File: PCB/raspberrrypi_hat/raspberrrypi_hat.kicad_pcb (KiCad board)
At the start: 4 copper layers, 65 x 56 mm, 24 parts, among them J3 40HAT, J6 CONN_02X02, J9 CONN_01X02, Q1 DMG2305UX, Q2 DMMT5401, U1 NeowayM590, U2 CAT24C32

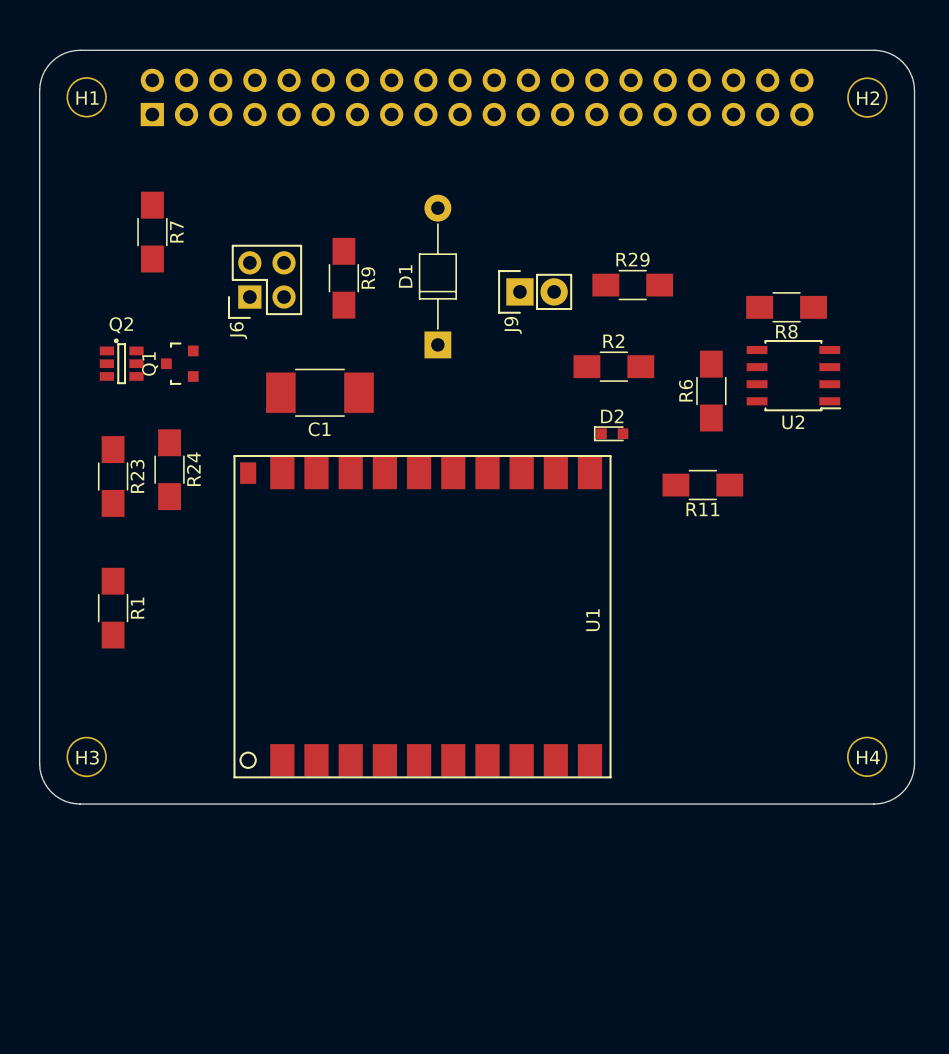
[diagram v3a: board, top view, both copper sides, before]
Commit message: PCB: Change RPi header + add Micro SIM socket. Starting placement
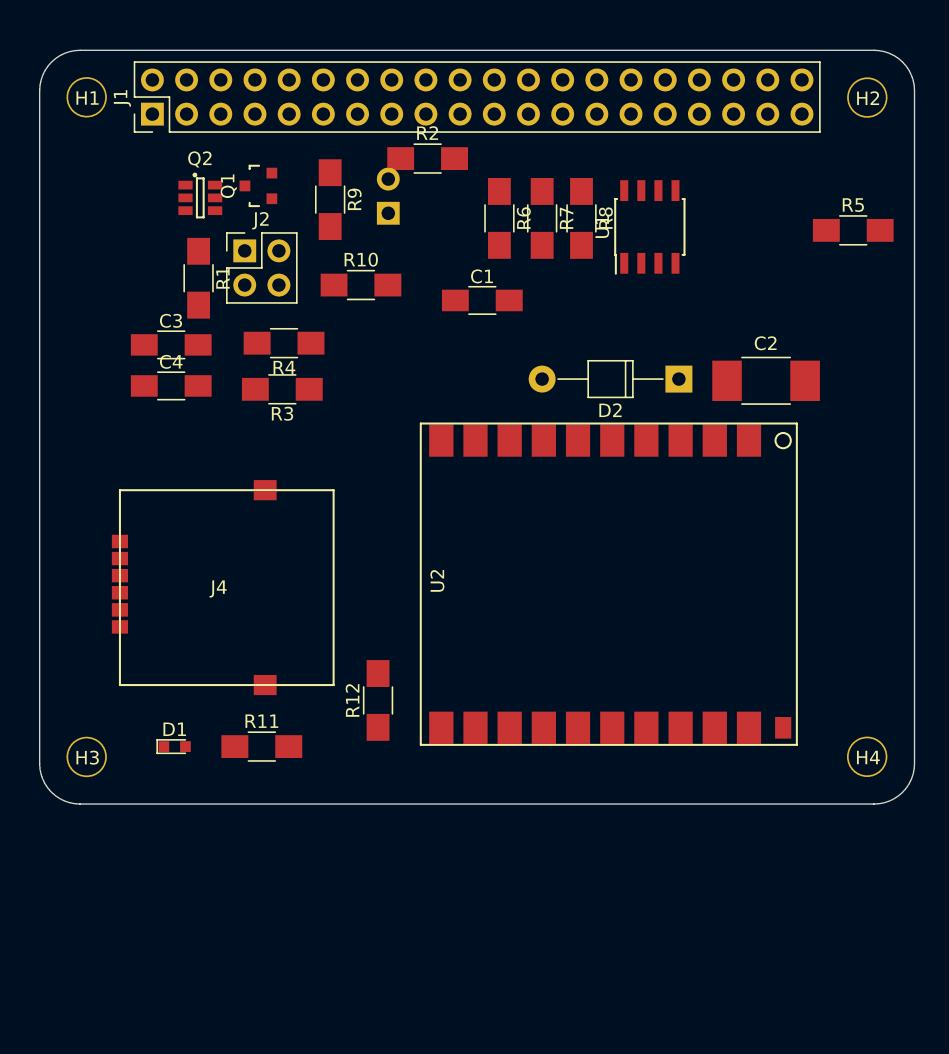
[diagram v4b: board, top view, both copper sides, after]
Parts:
- removed J6: CONN_02X02, Pin_Headers:Pin_Header_Straight_2x02
- removed J9: CONN_01X02, Pin_Headers:Pin_Header_Straight_1x02
- removed R23, R24: 22, Resistors_SMD:R_1206_HandSoldering
- removed R29: 10K, Resistors_SMD:R_1206_HandSoldering
- added C2: 470µF, Capacitors_SMD:C_1812_HandSoldering, F.Cu at (132.5, 85.4)
- added C3: 0.1µF, Capacitors_SMD:C_1206_HandSoldering, F.Cu at (88.3, 82.7)
- added C4: 100pF, Capacitors_SMD:C_1206_HandSoldering, F.Cu at (88.3, 85.8)
- added J1: 40HAT, Pin_Headers:Pin_Header_Straight_2x20_Pitch2.54mm, F.Cu at (86.9, 65.6)
- added J2: CONN_02X02, Pin_Headers:Pin_Header_Straight_2x02_Pitch2.54mm, F.Cu at (93.8, 75.7)
- added J4: Micro_SIM_Card, project_footprints:MicroSIMSocket, F.Cu at (84.5, 100.7)
- added R10: 200, Resistors_SMD:R_1206_HandSoldering, F.Cu at (102.4, 78.3)
- added R12: 10K, Resistors_SMD:R_1206_HandSoldering, F.Cu at (103.7, 109.1)
- added R3: DNP, Resistors_SMD:R_1206_HandSoldering, F.Cu at (96.6, 86.0)
- added R4: DNP, Resistors_SMD:R_1206_HandSoldering, F.Cu at (96.7, 82.6)
- added R5: DNP, Resistors_SMD:R_1206_HandSoldering, F.Cu at (139.0, 74.2)
- C1: value CP -> 100pF; footprint Capacitors_SMD:C_1812_HandSoldering -> Capacitors_SMD:C_1206_HandSoldering
- D1: value D -> LED; footprint Diodes_ThroughHole:D_T-1_P10.16mm_Horizontal -> LEDs:LED_0603
- D2: value LED -> 1N4007; footprint LEDs:LED_0603 -> Diodes_ThroughHole:D_T-1_P10.16mm_Horizontal
- J3: value 40HAT -> CONN_01X02; footprint Socket_Strips:Socket_Strip_Straight_2x20 -> Pin_Headers:Pin_Header_Straight_1x02_Pitch2.54mm
- R1, R2: value R -> 22
- R11: value DNP -> 4.7K
- R6: value 3.9K -> 10K
- R7: value DNP -> 3.9K
- R9: value DNP -> 200
- U1: value NeowayM590 -> CAT24C32; footprint project_footprints:NeowayM590 -> Housings_SOIC:SOIC-8_3.9x4.9mm_Pitch1.27mm
- U2: value CAT24C32 -> NeowayM590; footprint Housings_SOIC:SOIC-8_3.9x4.9mm_Pitch1.27mm -> project_footprints:NeowayM590
- moved U1 48.1 mm to (123.9, 73.9)
- moved R11 38.1 mm to (95.1, 112.5), turned to 0 degrees
- moved D1 35.7 mm to (88.6, 112.5), turned to 0 degrees
- moved R7 29.0 mm to (115.9, 73.3)
- moved R1 25.3 mm to (90.4, 77.8)
- moved R2 20.7 mm to (107.4, 68.9)
- moved R6 20.3 mm to (112.7, 73.3), turned to 270 degrees
- moved J3 19.0 mm to (104.5, 72.9)
- moved R8 16.6 mm to (118.8, 73.3), turned to 270 degrees
- moved Q1 14.4 mm to (94.8, 70.9)
- moved C1 13.9 mm to (111.4, 79.4), turned to 0 degrees
- moved Q2 13.6 mm to (90.5, 71.8)
- moved D2 6.41 mm to (126.0, 85.2), turned to 180 degrees
- moved R9 5.93 mm to (100.1, 71.9)
- moved U2 5.85 mm to (131.2, 89.8), turned to 270 degrees
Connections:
- C1 pad 1: Net-(C1-Pad1) -> /RXD
- D1 pad 1: Net-(C1-Pad1) -> GND
- D1 pad 2: /P5V -> Net-(D1-Pad2)
- D2 pad 1: GND -> /M590/VBAT
- D2 pad 2: Net-(D2-Pad2) -> /P5V
- J3 pad 1: /P3V3_HAT -> GND
- J3 pad 2: /P5V_HAT -> Net-(J3-Pad2)
- R1 pad 1: (no net) -> Net-(Q2-Pad1)
- R1 pad 2: (no net) -> GND
- R11 pad 1: Net-(J9-Pad2) -> Net-(R11-Pad1)
- R11 pad 2: GND -> Net-(D1-Pad2)
- R2 pad 1: (no net) -> Net-(Q1-Pad1)
- R2 pad 2: Net-(D2-Pad2) -> GND
- R6 pad 2: /ID_SD_EEPROM -> Net-(J3-Pad2)
- R7 pad 1: /P3V3_HAT -> /P3V3
- R7 pad 2: /P3V3 -> /ID_SD_EEPROM
- R9 pad 1: /P5V_HAT -> /TXD
- R9 pad 2: /P5V -> /TXD
- U1 pad 2: /P5V -> GND
- U1 pad 3: /P5V -> GND
- U1 pad 4: (no net) -> GND
- U1 pad 5: (no net) -> /ID_SC_EEPROM
- U1 pad 6: (no net) -> /ID_SD_EEPROM
- U1 pad 7: (no net) -> Net-(J3-Pad2)
- U1 pad 8: (no net) -> /P3V3
- U2 pad 2: GND -> /M590/VBAT
- U2 pad 3: GND -> /M590/VBAT
- U2 pad 5: /ID_SC_EEPROM -> Net-(R11-Pad1)
- U2 pad 6: /ID_SD_EEPROM -> (no net)
- U2 pad 7: Net-(J9-Pad2) -> /RXD
- U2 pad 8: /P3V3 -> /TXD
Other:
- board text removed: "If you want to use an SMT 40-pin header, please move the top edge up by 0.5mm and locate the header in the same location as the current TH part."

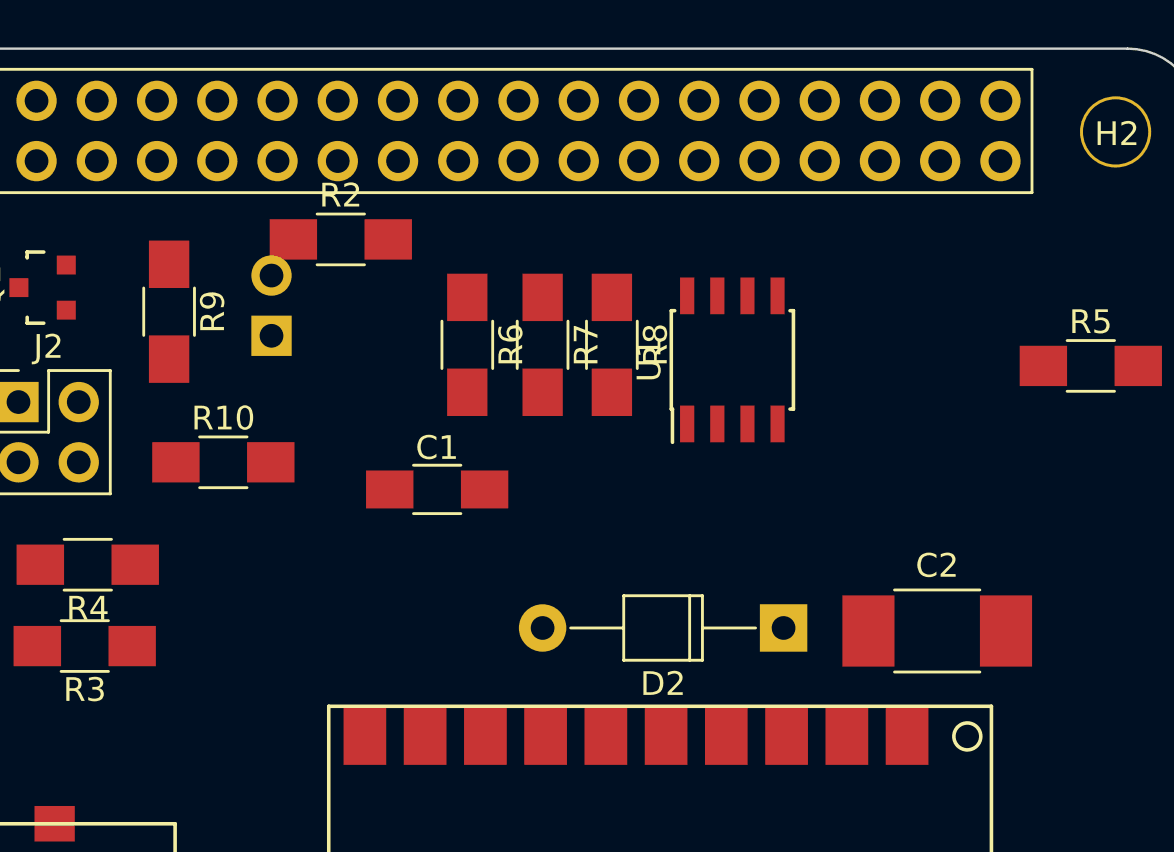
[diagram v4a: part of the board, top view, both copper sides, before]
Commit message: Fix TX/RX serial resistor short-cut by adding mTX/mRX in M590 module sheet
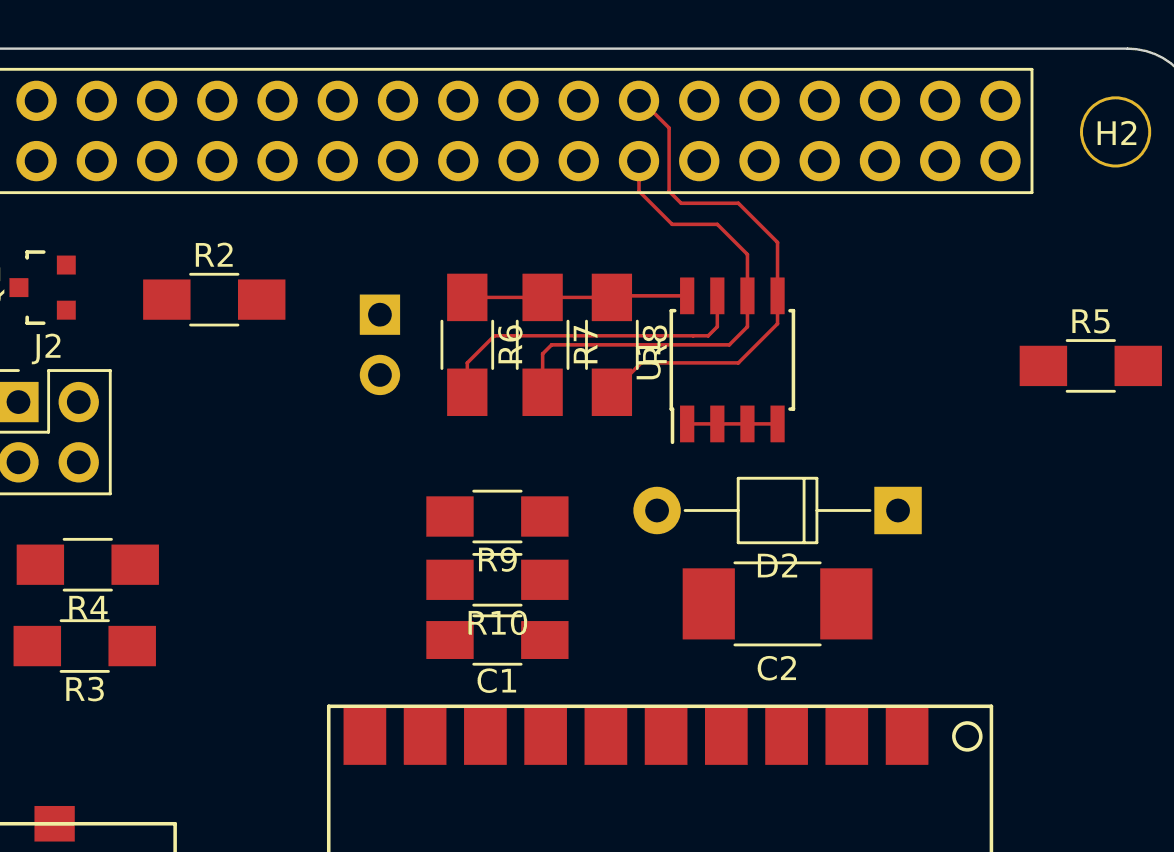
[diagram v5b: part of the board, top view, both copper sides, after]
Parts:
- moved R9 16.3 mm to (114.0, 80.5), turned to 180 degrees
- moved R10 12.6 mm to (114.0, 83.2), turned to 180 degrees
- moved D2 6.92 mm to (130.9, 80.3)
- moved C1 6.84 mm to (114.0, 85.8), turned to 180 degrees
- moved C2 6.83 mm to (125.8, 84.2), turned to 180 degrees
- moved R2 5.91 mm to (102.0, 71.4)
- moved J3 4.66 mm to (109.0, 72.0), turned to 180 degrees
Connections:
- C1 pad 1: /RXD -> /M590/mRXD
- R10 pad 1: /RXD -> /M590/mRXD
- R9 pad 1: /TXD -> /M590/mTXD
- U2 pad 7: /RXD -> /M590/mRXD
- U2 pad 8: /TXD -> /M590/mTXD
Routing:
- net /ID_SC_EEPROM: track 0.11 -> 21.6 mm
- net /ID_SD_EEPROM: track 1.07 -> 21.8 mm
- net Net-(J3-Pad2): track 0.00 -> 13.7 mm
- net /P3V3: track 0.00 -> 9.30 mm
- net GND: track 0.00 -> 3.81 mm

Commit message: PCB: keep on routing
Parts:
- J3: moved to F.Cu
- moved C3 46.0 mm to (133.3, 72.8)
- moved C4 45.9 mm to (133.2, 76.1)
- moved R5 22.9 mm to (116.8, 68.6), turned to 180 degrees
- moved D2 21.9 mm to (109.0, 79.1)
- moved R2 16.3 mm to (86.2, 75.0), turned to 180 degrees
- moved R4 8.31 mm to (88.8, 85.2), turned to 90 degrees
- moved J2 8.18 mm to (94.7, 83.8), turned to 270 degrees
- moved C1 6.04 mm to (119.8, 84.2), turned to 270 degrees
- moved R1 4.19 mm to (86.2, 77.6), turned to 180 degrees
- moved Q2 3.44 mm to (87.1, 71.5)
- moved Q1 2.87 mm to (92.0, 71.5), turned to 0 degrees
- moved R10 2.79 mm to (114.0, 86.0)
- moved R9 2.79 mm to (114.0, 83.3)
- moved R3 1.77 mm to (98.2, 85.4), turned to 90 degrees
- moved R11 0.25 mm to (95.3, 112.5), turned to 180 degrees
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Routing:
- net Net-(R11-Pad1): track 0.00 -> 72.9 mm
- net /M590/VBAT: track 0.00 -> 40.4 mm
- net /P3V3_HAT: track 0.00 -> 38.9 mm
- net Net-(J4-Pad1): track 0.00 -> 37.6 mm
- net Net-(J4-Pad2): track 0.00 -> 34.2 mm
- net /RXD: track 0.00 -> 31.6 mm
- net Net-(J4-Pad7): track 0.00 -> 31.5 mm
- net Net-(J4-Pad3): track 0.00 -> 30.0 mm
- net /TXD: track 0.00 -> 27.7 mm
- net /P5V_HAT: track 0.00 -> 24.0 mm
- net /P5V: track 0.00 -> 17.7 mm
- net /M590/mRXD: track 0.00 -> 10.9 mm
- net Net-(J3-Pad2): track 13.7 -> 24.0 mm
- net /M590/mTXD: track 0.00 -> 8.51 mm
- net Net-(Q1-Pad1): track 0.00 -> 5.41 mm
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
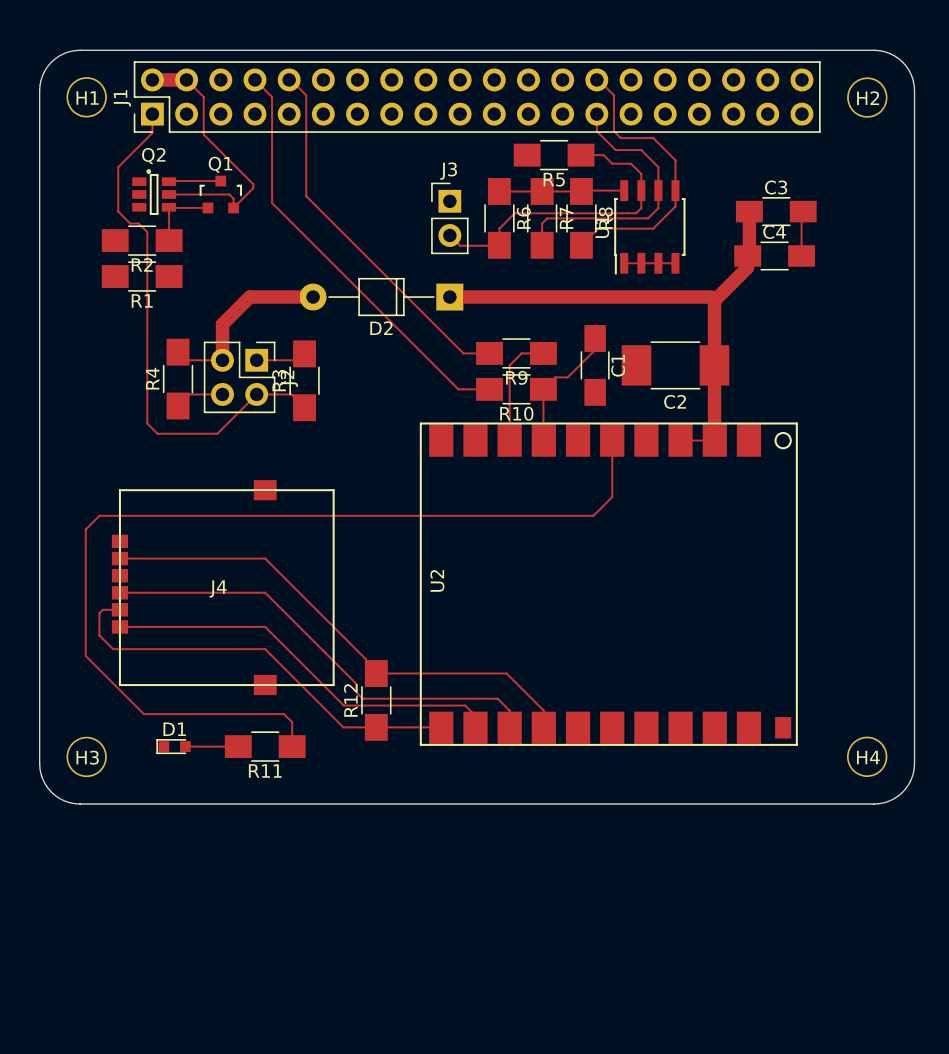
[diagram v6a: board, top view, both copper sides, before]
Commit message: PCB: routing completed. Reworked alim+eeprom. Add filled zones.
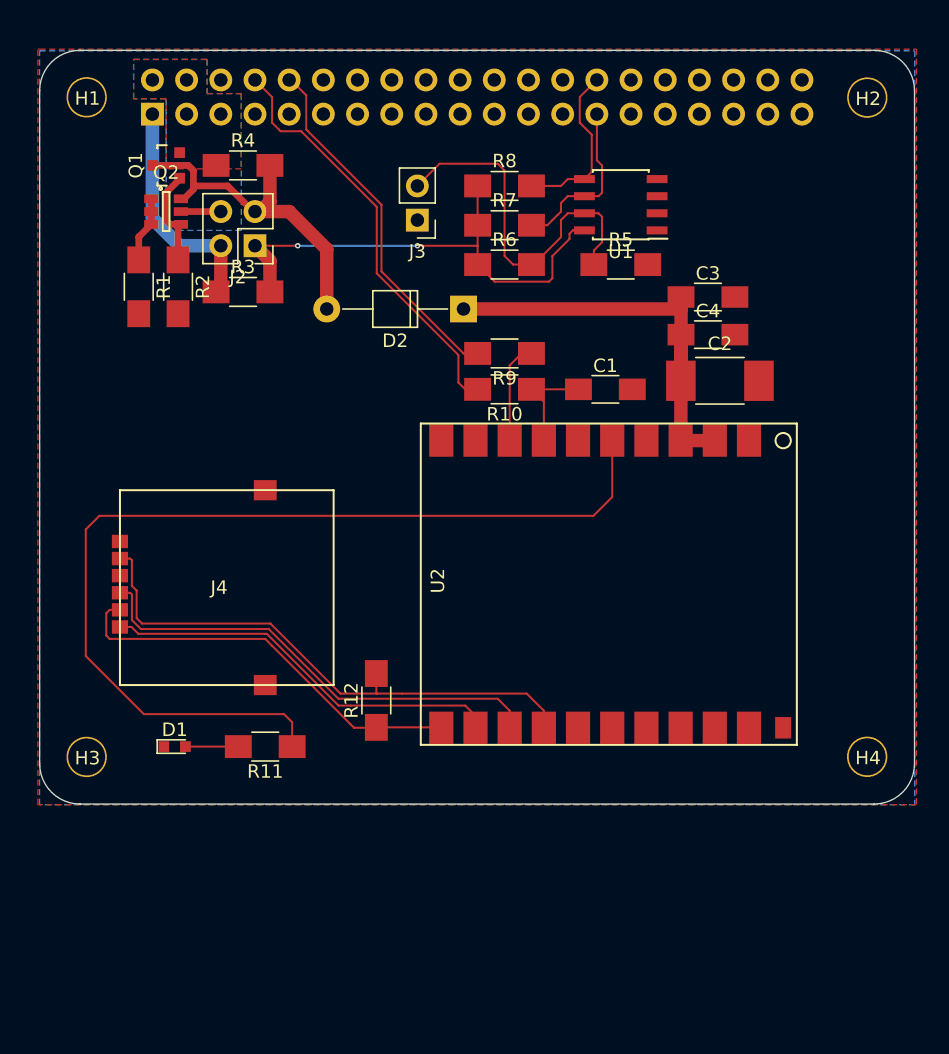
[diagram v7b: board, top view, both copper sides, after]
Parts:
- J1: footprint Pin_Headers:Pin_Header_Straight_2x20_Pitch2.54mm -> Socket_Strips:Socket_Strip_Straight_2x20_Pitch2.54mm; moved to B.Cu
- moved R4 16.6 mm to (93.7, 69.4), turned to 0 degrees
- moved R5 9.52 mm to (121.7, 76.7), turned to 0 degrees
- moved J2 8.51 mm to (94.5, 75.3), turned to 180 degrees
- moved C3 8.13 mm to (128.2, 79.1)
- moved R3 8.03 mm to (93.7, 78.8), turned to 0 degrees
- moved C4 7.66 mm to (128.2, 81.9)
- moved R8 6.20 mm to (113.1, 70.9), turned to 0 degrees
- moved Q1 4.60 mm to (87.9, 69.4), turned to 90 degrees
- moved R2 4.34 mm to (88.8, 78.4), turned to 270 degrees
- moved C2 3.49 mm to (129.1, 85.4), turned to 0 degrees
- moved R6 3.45 mm to (113.1, 76.7), turned to 0 degrees
- moved R7 2.84 mm to (113.1, 73.8), turned to 0 degrees
- moved J3 2.79 mm to (106.6, 73.4), turned to 180 degrees
- moved U1 2.72 mm to (121.7, 72.3), turned to 180 degrees
- moved C1 1.93 mm to (120.6, 86.0), turned to 0 degrees
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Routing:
- net /P3V3: track 13.1 -> 39.0 mm, vias 0 -> 2
- net /P3V3_HAT: track 38.9 -> 17.2 mm
- net /P5V_HAT: track 24.0 -> 2.96 mm
- net /P5V: track 17.7 -> 26.7 mm
- net /ID_SC_EEPROM: track 21.6 -> 12.7 mm
- net /M590/VBAT: track 40.4 -> 32.9 mm
- net /ID_SD_EEPROM: track 21.8 -> 14.3 mm
- net GND: track 7.16 -> 0.00 mm
- net Net-(Q2-Pad1): track 0.00 -> 4.92 mm
- net Net-(J4-Pad1): track 37.6 -> 42.3 mm
- net Net-(J3-Pad2): track 24.0 -> 27.5 mm
- net /M590/mRXD: track 10.9 -> 7.78 mm
- net Net-(Q1-Pad1): track 5.41 -> 7.48 mm
- net Net-(J4-Pad7): track 31.5 -> 30.5 mm
- net /TXD: track 27.7 -> 26.8 mm
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- added copper zone on B.Cu, net /P5V_HAT
- added copper zone on F.Cu, net /P5V_HAT
- added copper zone on B.Cu, net GND
- added copper zone on F.Cu, net GND
